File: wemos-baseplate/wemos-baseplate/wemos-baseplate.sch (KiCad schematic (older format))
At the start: 3 parts, among them U1 ESP32-MINI-32, U2 ESP32-MINI-32, U3 ESP32-MINI-32

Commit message: footprint OK
horizontal lines set
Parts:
- U1, U2, U3: symbol in2tech:ESP32-MINI-32 -> wemos-baseplate-rescue:ESP32-MINI-32-in2tech
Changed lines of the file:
@@
 GND
 $Comp
-L in2tech:ESP32-MINI-32 U1
+L wemos-baseplate-rescue:ESP32-MINI-32-in2tech U1
 U 1 1 5E32E116
 P 3125 4675
@@
 GND
 $Comp
-L in2tech:ESP32-MINI-32 U2
+L wemos-baseplate-rescue:ESP32-MINI-32-in2tech U2
 U 1 1 5E33F0D3
 P 4925 4675
@@
 GND
 $Comp
-L in2tech:ESP32-MINI-32 U3
+L wemos-baseplate-rescue:ESP32-MINI-32-in2tech U3
 U 1 1 5E341442
 P 6800 4675

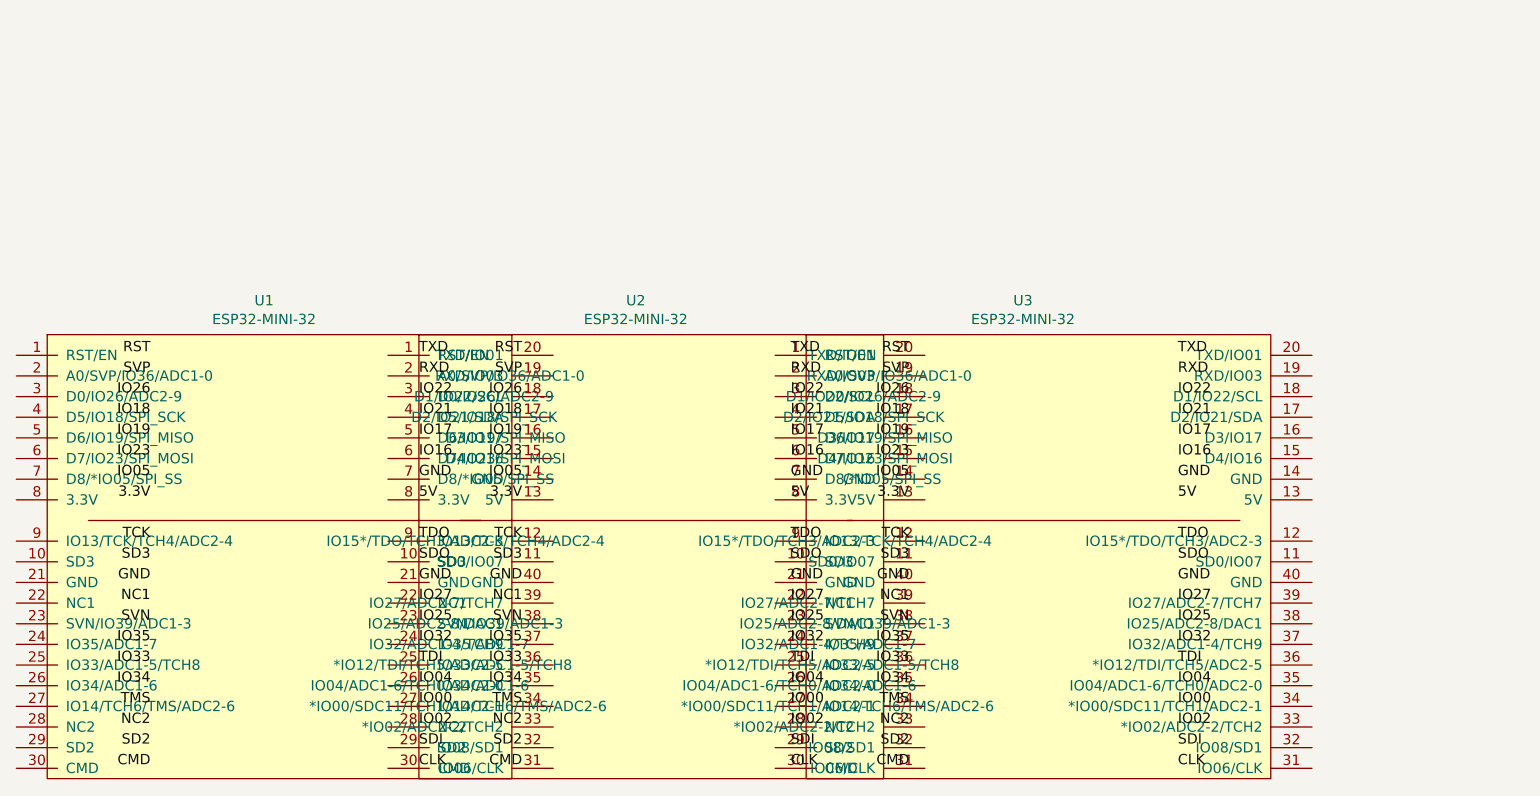
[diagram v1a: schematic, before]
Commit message: corrected lib
added spreadsheet with PinMapping
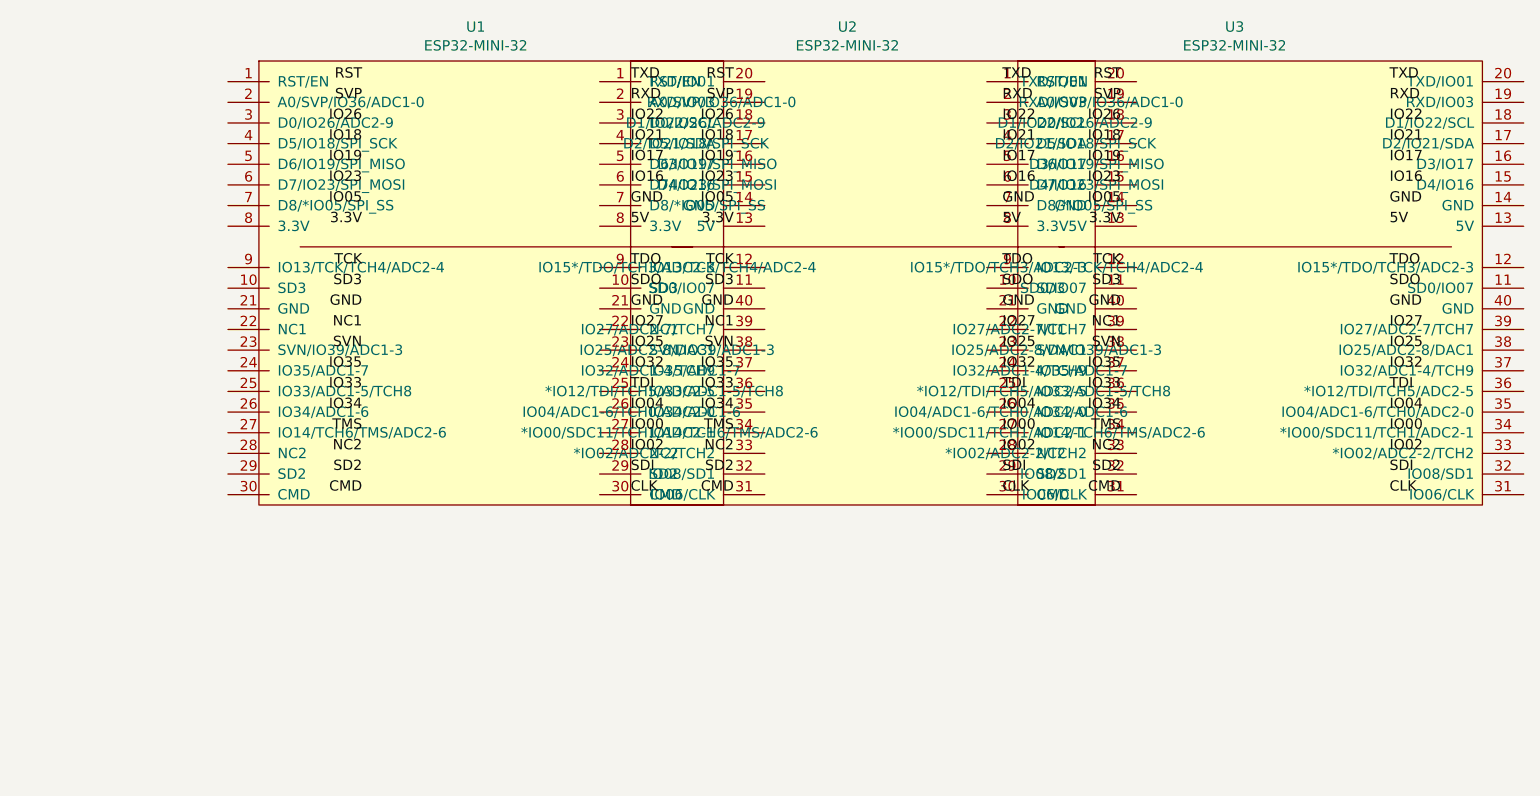
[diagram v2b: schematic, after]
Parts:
- U1, U2, U3: Spice_Netlist_Enabled (none) -> Y; Spice_Primitive (none) -> I
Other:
- moved on the sheet: U1, U2, U3

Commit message: 1st print layout with i2c/grove and extention connectors
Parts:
- added J1, J6: Conn_02x20_Odd_Even, Connector_PinSocket_2.54mm:PinSocket_2x20_P2.54mm_Vertical, symbol Connector_Generic:Conn_02x20_Odd_Even
- added J2, J3, J4, J5: Conn_01x04, Connectors:Grove_1x04, symbol Connector_Generic:Conn_01x04
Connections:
- net labels added: +3.3V, +5C, GNDPWR, SCL, SDA
- net labels removed: IO21, IO22
- wire segments 0 -> 3
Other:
- moved on the sheet: U1, U2, U3

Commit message: versie met 30 pinnen in connector
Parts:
- removed J1, J6: Conn_02x20_Odd_Even, Connector_PinSocket_2.54mm:PinSocket_2x20_P2.54mm_Vertical, symbol Connector_Generic:Conn_02x20_Odd_Even
- added J1: Conn_02x16_Odd_Even, Connector_PinHeader_2.54mm:PinHeader_2x16_P2.54mm_Horizontal, symbol Connector_Generic:Conn_02x16_Odd_Even
- added J2: Conn_02x16_Odd_Even, Connector_PinSocket_2.54mm:PinSocket_2x16_P2.54mm_Horizontal, symbol Connector_Generic:Conn_02x16_Odd_Even
- renumbered J2 to J6
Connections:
- net labels added: SD0, SD1
- net labels removed: SDI, SDO
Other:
- moved on the sheet: J4, J6, U1

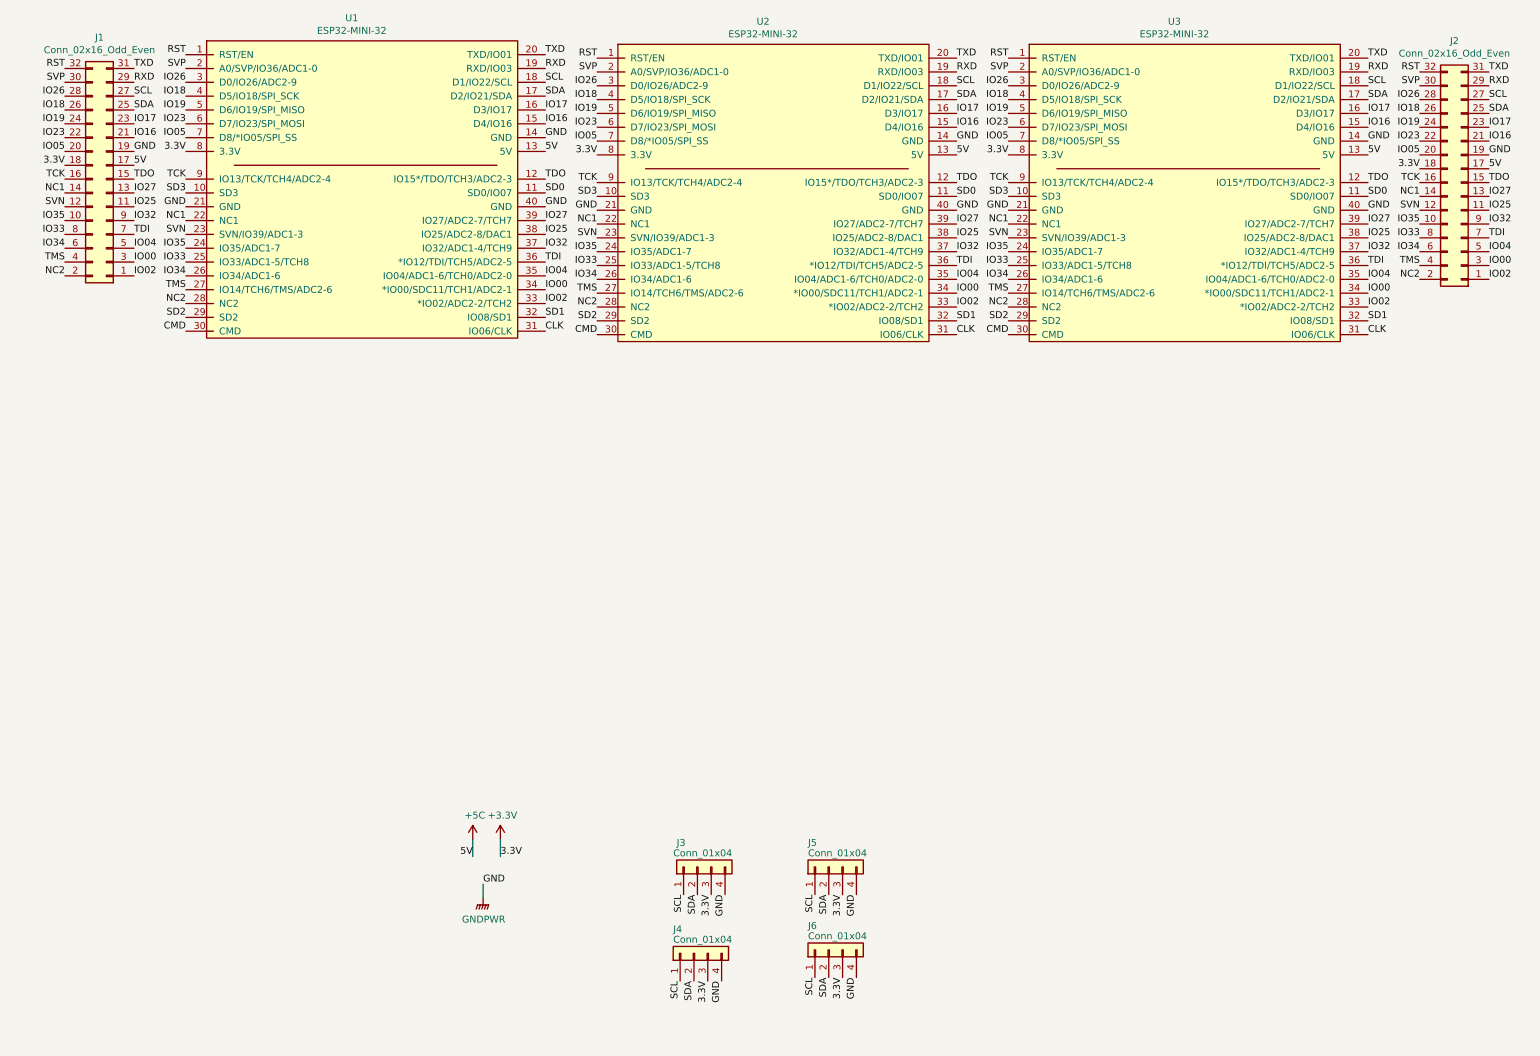
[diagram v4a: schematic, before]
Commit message: added grove connectors
added labels for grove connectors
added filled area's for ground and 3v3 plane
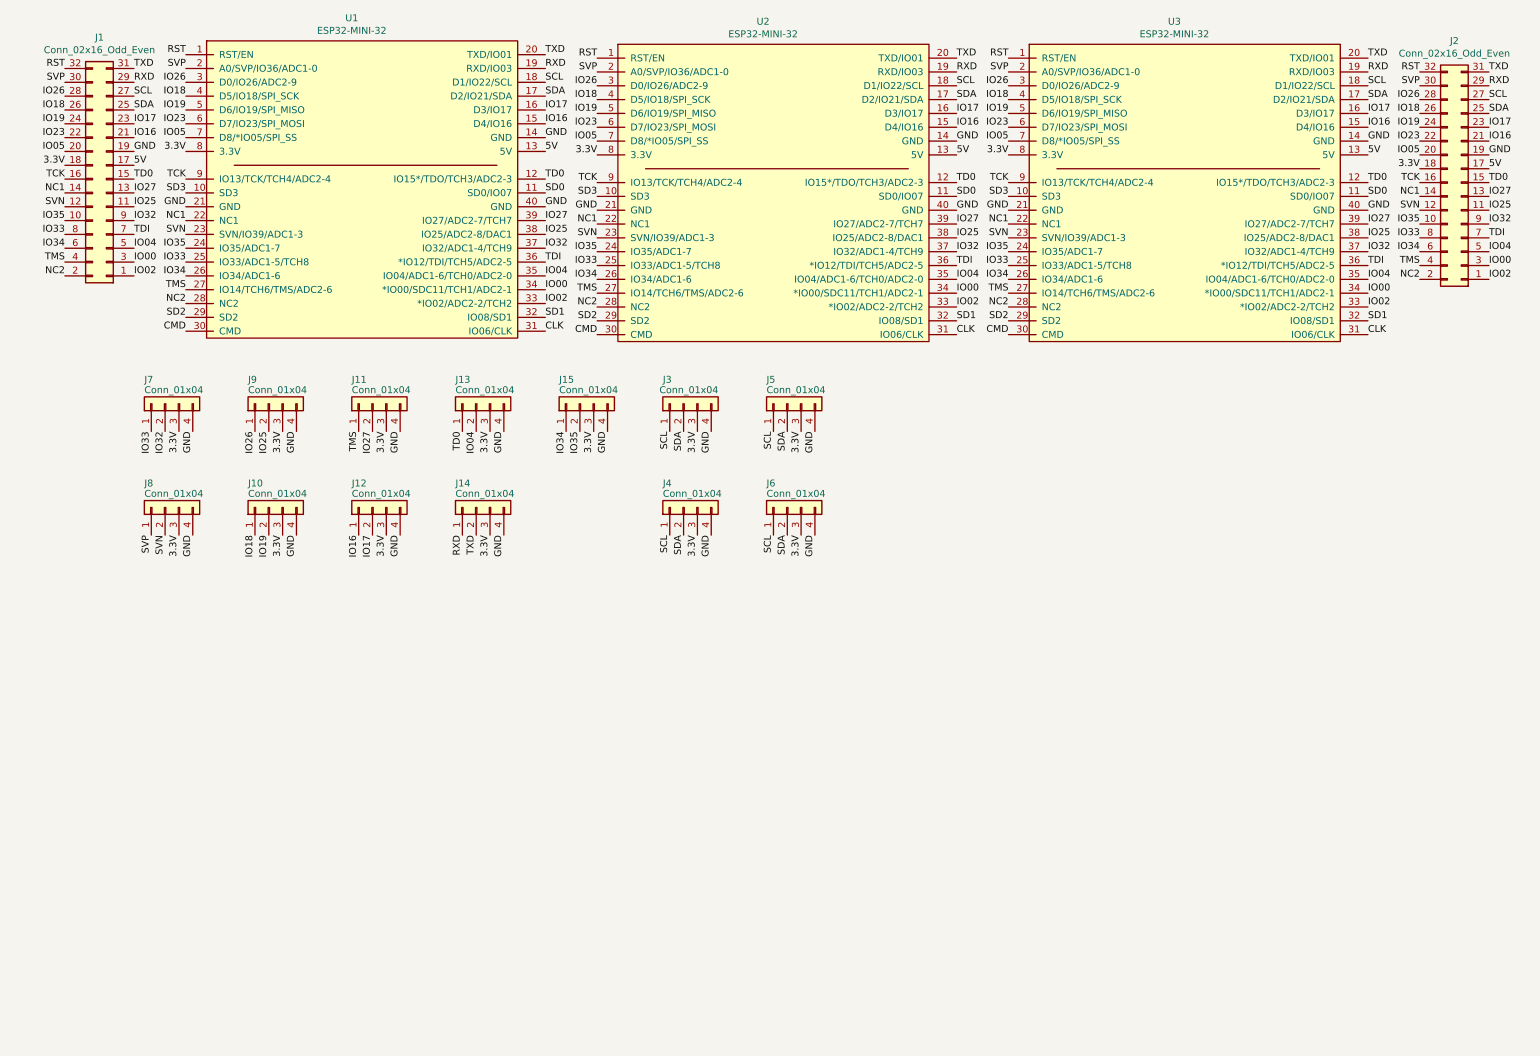
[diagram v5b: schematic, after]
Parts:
- added J10, J11, J12, J13, J14, J15, J7, J8, J9: Conn_01x04, Connectors:Grove_1x04, symbol Connector_Generic:Conn_01x04
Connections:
- net IO04: now also J13.2 (Pin_2)
- net IO16: now also J12.1 (Pin_1)
- net IO17: now also J12.2 (Pin_2)
- net IO18: now also J10.1 (Pin_1)
- net IO19: now also J10.2 (Pin_2)
- net IO25: now also J9.2 (Pin_2)
- net IO26: now also J9.1 (Pin_1)
- net IO27: now also J11.2 (Pin_2)
- net IO32: now also J7.2 (Pin_2)
- net IO33: now also J7.1 (Pin_1)
- net IO34: now also J15.1 (Pin_1)
- net IO35: now also J15.2 (Pin_2)
- net RXD: now also J14.1 (Pin_1)
- net SVN: now also J8.2 (Pin_2)
- net SVP: now also J8.1 (Pin_1)
- net TMS: now also J11.1 (Pin_1)
- net TXD: now also J14.2 (Pin_2)
- net +3V3 renamed 3.3V
- net 3.3V: now also J10.3 (Pin_3), J11.3 (Pin_3), J12.3 (Pin_3), J13.3 (Pin_3), J14.3 (Pin_3), J15.3 (Pin_3), J7.3 (Pin_3), J8.3 (Pin_3), J9.3 (Pin_3)
- net +5C renamed 5V
- net GNDPWR renamed GND
- net GND: now also J10.4 (Pin_4), J11.4 (Pin_4), J12.4 (Pin_4), J13.4 (Pin_4), J14.4 (Pin_4), J15.4 (Pin_4), J7.4 (Pin_4), J8.4 (Pin_4), J9.4 (Pin_4)
- net TDO renamed TD0
- net TD0: now also J13.1 (Pin_1)
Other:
- moved on the sheet: J3, J4, J5, J6

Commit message: corrected library, still a few nets on the board to fix
in2tech library in separate path
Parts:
- J1: footprint Connector_PinHeader_2.54mm:PinHeader_2x16_P2.54mm_Horizontal -> in2tech:PinHeader_2x16_P2.54mm_Horizontal_oval
- J10, J11, J12, J13, J14, J15, J3, J4, J5, J6, J9: footprint Connectors:Grove_1x04 -> in2tech:Grove_1x04_oval
- J2: footprint Connector_PinSocket_2.54mm:PinSocket_2x16_P2.54mm_Horizontal -> in2tech:PinSocket_2x16_P2.54mm_Horizontal_oval
- U1, U2, U3: symbol wemos-baseplate-rescue:ESP32-MINI-32-in2tech -> in2tech2:ESP32-MINI-32
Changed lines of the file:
@@
 GND
 $Comp
-L wemos-baseplate-rescue:ESP32-MINI-32-in2tech U1
+L in2tech2:ESP32-MINI-32 U1
 U 1 1 5E32E116
 P 2850 1675
 F 0 "U1" H 2750 2840 50  0000 C CNN
 F 1 "ESP32-MINI-32" H 2750 2749 50  0000 C CNN
-F 2 "in2tech:QIP-40_1000_ELL" H 2850 1575 50  0001 C CNN
+F 2 "in2tech:QIP-40_1000_ELL" H 2850 1575 50  0000 C CNN
 F 3 "" H 2850 1575 50  0001 C CNN
 F 4 "Y" H 2850 1675 50  0001 C CNN "Spice_Netlist_Enabled"
@@
 GND
 $Comp
-L wemos-baseplate-rescue:ESP32-MINI-32-in2tech U2
+L in2tech2:ESP32-MINI-32 U2
 U 1 1 5E33F0D3
 P 5825 1700
@@
 GND
 $Comp
-L wemos-baseplate-rescue:ESP32-MINI-32-in2tech U3
+L in2tech2:ESP32-MINI-32 U3
 U 1 1 5E341442
 P 8800 1700
@@
 F 0 "J3" V 5325 3450 50  0000 R CNN
 F 1 "Conn_01x04" V 5250 3475 50  0000 R CNN
-F 2 "Connectors:Grove_1x04" H 5150 3300 50  0001 C CNN
+F 2 "in2tech:Grove_1x04_oval" H 5150 3300 50  0001 C CNN
 F 3 "~" H 5150 3300 50  0001 C CNN
 	1    5150 3300
@@
 F 0 "J5" V 6075 3450 50  0000 R CNN
 F 1 "Conn_01x04" V 6000 3450 50  0000 R CNN
-F 2 "Connectors:Grove_1x04" H 5900 3300 50  0001 C CNN
+F 2 "in2tech:Grove_1x04_oval" H 5900 3300 50  0001 C CNN
 F 3 "~" H 5900 3300 50  0001 C CNN
 	1    5900 3300
@@
 F 0 "J6" V 6075 4200 50  0000 R CNN
 F 1 "Conn_01x04" V 6000 4200 50  0000 R CNN
-F 2 "Connectors:Grove_1x04" H 5900 4050 50  0001 C CNN
+F 2 "in2tech:Grove_1x04_oval" H 5900 4050 50  0001 C CNN
 F 3 "~" H 5900 4050 50  0001 C CNN
 	1    5900 4050
@@
 F 0 "J4" V 5325 4200 50  0000 R CNN
 F 1 "Conn_01x04" V 5250 4200 50  0000 R CNN
-F 2 "Connectors:Grove_1x04" H 5150 4050 50  0001 C CNN
+F 2 "in2tech:Grove_1x04_oval" H 5150 4050 50  0001 C CNN
 F 3 "~" H 5150 4050 50  0001 C CNN
 	1    5150 4050
@@
 F 0 "J1" H 1025 650 50  0000 C CNN
 F 1 "Conn_02x16_Odd_Even" H 1025 741 50  0000 C CNN
-F 2 "Connector_PinHeader_2.54mm:PinHeader_2x16_P2.54mm_Horizontal" H 975 1675 50  0001 C CNN
+F 2 "in2tech:PinHeader_2x16_P2.54mm_Horizontal_oval" H 975 1675 50  0001 C CNN
 F 3 "~" H 975 1675 50  0001 C CNN
 	1    975  1675
@@
 F 0 "J2" H 10825 675 50  0000 C CNN
 F 1 "Conn_02x16_Odd_Even" H 10825 766 50  0000 C CNN
-F 2 "Connector_PinSocket_2.54mm:PinSocket_2x16_P2.54mm_Horizontal" H 10775 1700 50  0001 C CNN
+F 2 "in2tech:PinSocket_2x16_P2.54mm_Horizontal_oval" H 10775 1700 50  0001 C CNN
 F 3 "~" H 10775 1700 50  0001 C CNN
 	1    10775 1700
@@
 F 0 "J9" V 2325 3450 50  0000 R CNN
 F 1 "Conn_01x04" V 2250 3450 50  0000 R CNN
-F 2 "Connectors:Grove_1x04" H 2150 3300 50  0001 C CNN
+F 2 "in2tech:Grove_1x04_oval" H 2150 3300 50  0001 C CNN
 F 3 "~" H 2150 3300 50  0001 C CNN
 	1    2150 3300
@@
 F 0 "J11" V 3075 3450 50  0000 R CNN
 F 1 "Conn_01x04" V 3000 3450 50  0000 R CNN
-F 2 "Connectors:Grove_1x04" H 2900 3300 50  0001 C CNN
+F 2 "in2tech:Grove_1x04_oval" H 2900 3300 50  0001 C CNN
 F 3 "~" H 2900 3300 50  0001 C CNN
 	1    2900 3300
@@
 F 0 "J13" V 3825 3450 50  0000 R CNN
 F 1 "Conn_01x04" V 3750 3450 50  0000 R CNN
-F 2 "Connectors:Grove_1x04" H 3650 3300 50  0001 C CNN
+F 2 "in2tech:Grove_1x04_oval" H 3650 3300 50  0001 C CNN
 F 3 "~" H 3650 3300 50  0001 C CNN
 	1    3650 3300
@@
 F 0 "J15" V 4575 3450 50  0000 R CNN
 F 1 "Conn_01x04" V 4500 3450 50  0000 R CNN
-F 2 "Connectors:Grove_1x04" H 4400 3300 50  0001 C CNN
+F 2 "in2tech:Grove_1x04_oval" H 4400 3300 50  0001 C CNN
 F 3 "~" H 4400 3300 50  0001 C CNN
 	1    4400 3300
@@
 F 0 "J10" V 2325 4200 50  0000 R CNN
 F 1 "Conn_01x04" V 2250 4200 50  0000 R CNN
-F 2 "Connectors:Grove_1x04" H 2150 4050 50  0001 C CNN
+F 2 "in2tech:Grove_1x04_oval" H 2150 4050 50  0001 C CNN
 F 3 "~" H 2150 4050 50  0001 C CNN
 	1    2150 4050
@@
 F 0 "J12" V 3075 4200 50  0000 R CNN
 F 1 "Conn_01x04" V 3000 4200 50  0000 R CNN
-F 2 "Connectors:Grove_1x04" H 2900 4050 50  0001 C CNN
+F 2 "in2tech:Grove_1x04_oval" H 2900 4050 50  0001 C CNN
 F 3 "~" H 2900 4050 50  0001 C CNN
 	1    2900 4050
@@
 F 0 "J14" V 3825 4200 50  0000 R CNN
 F 1 "Conn_01x04" V 3750 4200 50  0000 R CNN
-F 2 "Connectors:Grove_1x04" H 3650 4050 50  0001 C CNN
+F 2 "in2tech:Grove_1x04_oval" H 3650 4050 50  0001 C CNN
 F 3 "~" H 3650 4050 50  0001 C CNN
 	1    3650 4050

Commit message: - Revised wemos-base-plate -  ground planes to top and bottom -  all tracks to 0.3 mm -  proper mounting holes in edges -  measurements to (not used) front adhesive layer -  front sik screen layout changed -  misc small clean up
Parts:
- added MH1, MH2, MH3, MH4: MountingHole, MountingHole:MountingHole_3.2mm_M3, symbol Mechanical:MountingHole
- U1, U2, U3: symbol in2tech2:ESP32-MINI-32 -> in2tech:ESP32-MINI-32
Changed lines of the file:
@@
 EESchema Schematic File Version 4
-EELAYER 30 0
+LIBS:wemos-baseplate-cache
+EELAYER 26 0
 EELAYER END
 $Descr A4 11693 8268
 encoding utf-8
 Sheet 1 1
-Title ""
-Date ""
-Rev ""
-Comp ""
-Comment1 ""
-Comment2 ""
+Title "Wemos-ESP32-Base Plate"
+Date "2020-02-09"
+Rev "1.1"
+Comp "Sensemakers Amsterdam"
+Comment1 "Revisions: Gijs Mos"
+Comment2 "Author: Karijn Wessing"
 Comment3 ""
 Comment4 ""
@@
 GND
 $Comp
-L in2tech2:ESP32-MINI-32 U1
+L in2tech:ESP32-MINI-32 U1
 U 1 1 5E32E116
 P 2850 1675
@@
 GND
 $Comp
-L in2tech2:ESP32-MINI-32 U2
+L in2tech:ESP32-MINI-32 U2
 U 1 1 5E33F0D3
 P 5825 1700
@@
 GND
 $Comp
-L in2tech2:ESP32-MINI-32 U3
+L in2tech:ESP32-MINI-32 U3
 U 1 1 5E341442
 P 8800 1700
@@
 Text Label 3650 4250 3    50   ~ 0
 TXD
+$Comp
+L Mechanical:MountingHole MH1
+U 1 1 5E402162
+P 1025 7350
+F 0 "MH1" H 1125 7350 50  0000 L CNN
+F 1 "MountingHole" H 1125 7305 50  0001 L CNN
+F 2 "MountingHole:MountingHole_3.2mm_M3" H 1025 7350 50  0001 C CNN
+F 3 "~" H 1025 7350 50  0001 C CNN
+	1    1025 7350
+	1    0    0    -1
+$EndComp
+$Comp
+L Mechanical:MountingHole MH2
+U 1 1 5E40223A
+P 1850 7350
+F 0 "MH2" H 1950 7350 50  0000 L CNN
+F 1 "MountingHole" H 1950 7305 50  0001 L CNN
+F 2 "MountingHole:MountingHole_3.2mm_M3" H 1850 7350 50  0001 C CNN
+F 3 "~" H 1850 7350 50  0001 C CNN
+	1    1850 7350
+	1    0    0    -1
+$EndComp
+$Comp
+L Mechanical:MountingHole MH3
+U 1 1 5E402432
+P 2575 7350
+F 0 "MH3" H 2675 7350 50  0000 L CNN
+F 1 "MountingHole" H 2675 7305 50  0001 L CNN
+F 2 "MountingHole:MountingHole_3.2mm_M3" H 2575 7350 50  0001 C CNN
+F 3 "~" H 2575 7350 50  0001 C CNN
+	1    2575 7350
+	1    0    0    -1
+$EndComp
+$Comp
+L Mechanical:MountingHole MH4
+U 1 1 5E40257A
+P 3325 7350
+F 0 "MH4" H 3425 7350 50  0000 L CNN
+F 1 "MountingHole" H 3425 7305 50  0001 L CNN
+F 2 "MountingHole:MountingHole_3.2mm_M3" H 3325 7350 50  0001 C CNN
+F 3 "~" H 3325 7350 50  0001 C CNN
+	1    3325 7350
+	1    0    0    -1
+$EndComp
 $EndSCHEMATC
